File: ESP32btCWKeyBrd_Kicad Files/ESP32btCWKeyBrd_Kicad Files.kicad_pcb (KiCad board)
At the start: 2 copper layers, 85.8 x 44 mm, 20 parts, among them J1 CW Key Out, J2 3.5" TFT ILI9488, J3 Audio In Jack, J4 Conn_01x02_MountingPin, Q1 MMBT3904, Q2 MMBT3906, Q3 D4184, U1 ESP32-DEVKIT-V1

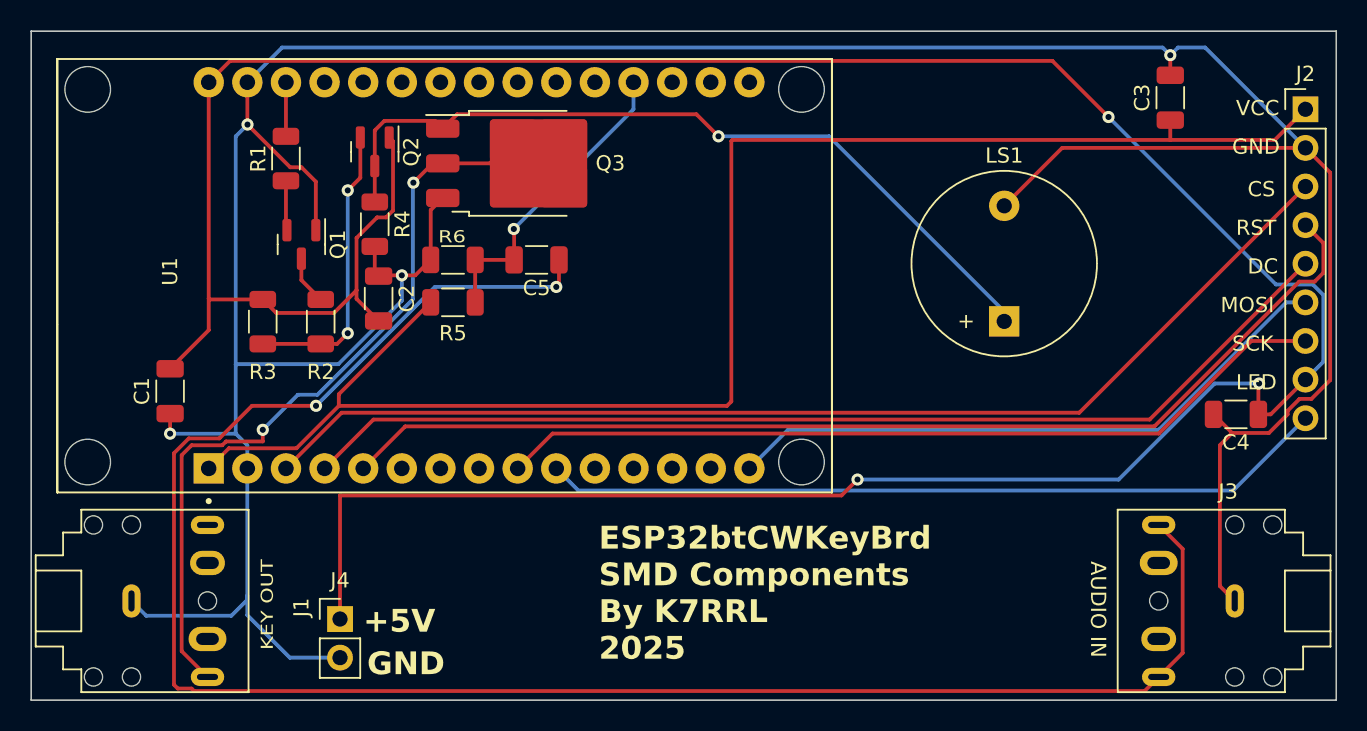
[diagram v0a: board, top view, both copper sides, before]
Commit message: Fixed the PCB
Unfortunately after I ordered the original set :(
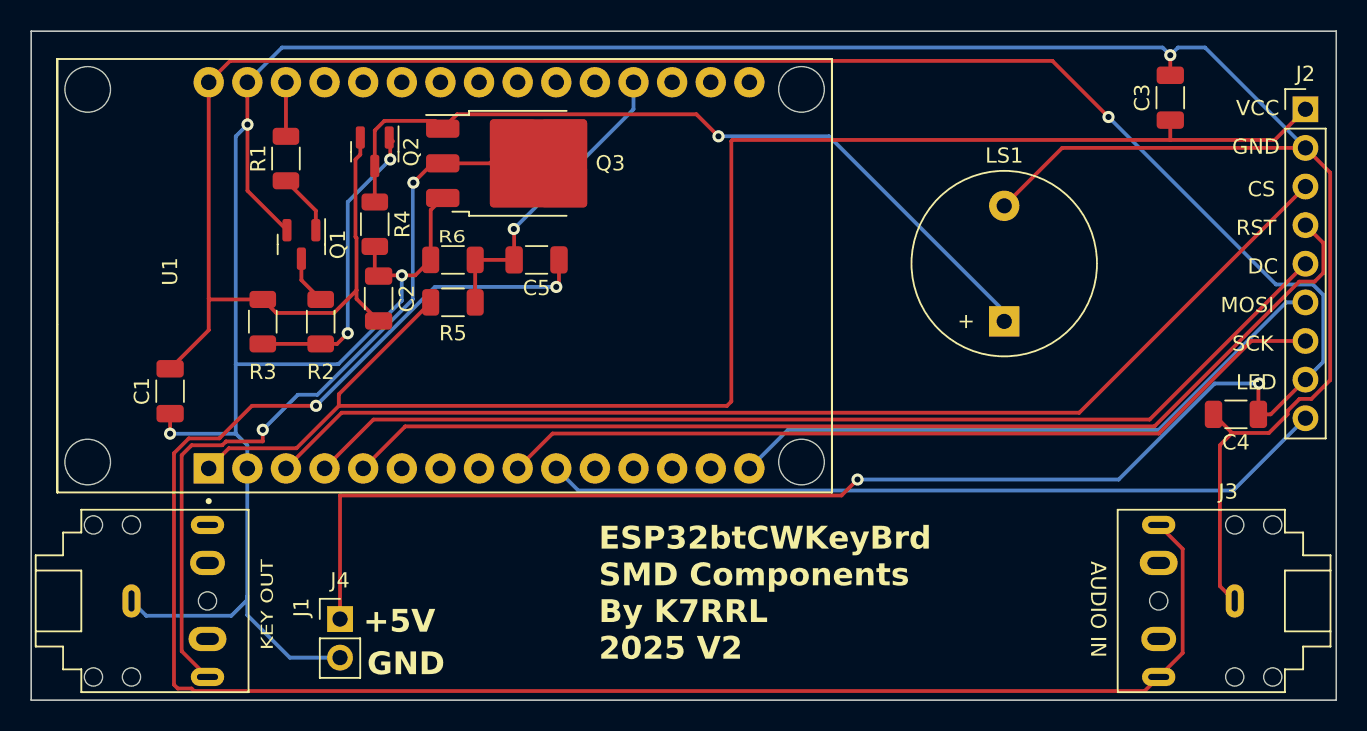
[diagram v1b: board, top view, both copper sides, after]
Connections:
- J4 pad 1: +5V -> Net-(J4-Pin_1)
- Q1 pad 1: GND -> Net-(Q1-B)
- Q1 pad 2: Net-(Q1-B) -> GND
- Q2 pad 1: +5V -> Net-(Q2-B)
- Q2 pad 2: Net-(Q2-B) -> +5V
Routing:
- net +5V: track 208.8 -> 207.5 mm
- net GND: track 225.1 -> 223.9 mm
- net Net-(Q2-B): track 19.1 -> 20.3 mm
- net Net-(Q1-B): track 3.28 -> 4.06 mm
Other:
- board text added: "ESP32btCWKeyBrd SMD Components By K7RRL 2025 V2"
- board text removed: "ESP32btCWKeyBrd SMD Components By K7RRL 2025"
